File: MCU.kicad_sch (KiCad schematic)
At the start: 15 parts, among them U5 STM32F405RGTx, Y1 12MHz

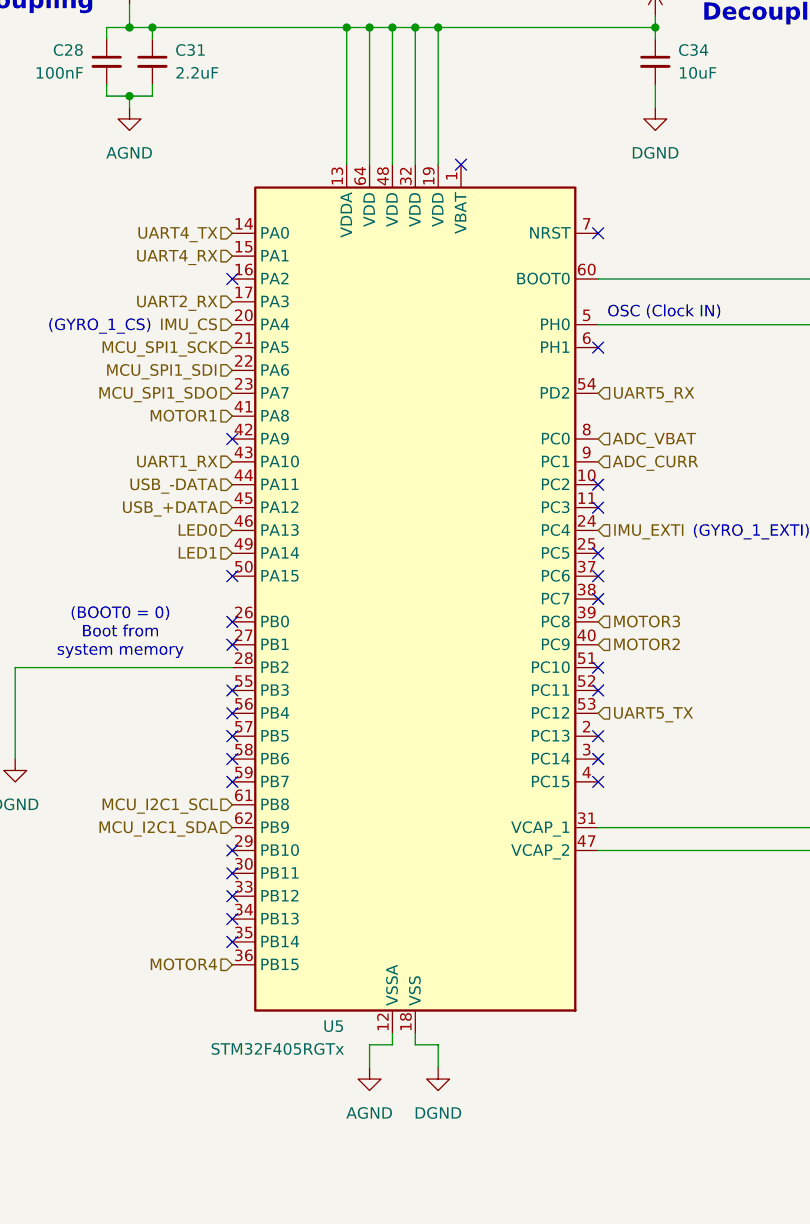
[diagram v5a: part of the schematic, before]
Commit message: More symbols updated to be compliant
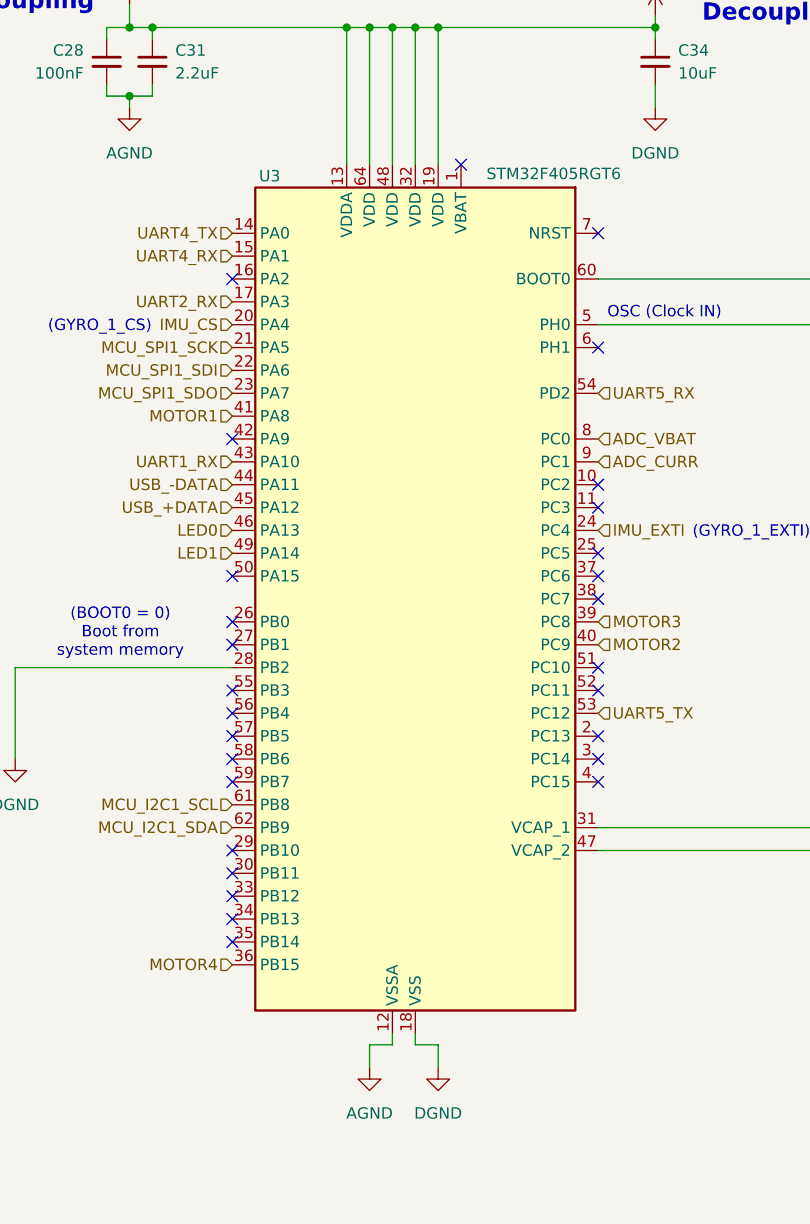
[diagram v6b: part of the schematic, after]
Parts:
- removed U5: STM32F405RGTx, Package_QFP:LQFP-64_10x10mm_P0.5mm, symbol MCU_ST_STM32F4:STM32F405RGTx
- added U3: STM32F405RGT6, Package_QFP:LQFP-64_10x10mm_P0.5mm, symbol KSE_MCU:STM32F405RGT6
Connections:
- net +3V3: now also U3.13 (VDDA), U3.19 (VDD), U3.32 (VDD), U3.48 (VDD), U3.64 (VDD)
- net ADC_CURR: now also U3.9 (PC1)
- net ADC_VBAT: now also U3.8 (PC0)
- net AGND: now also U3.12 (VSSA)
- net CLK_OUT: now also U3.5 (PH0)
- net DFU_Enable: now also U3.60 (BOOT0)
- net DGND: now also U3.18 (VSS), U3.28 (PB2), U3.63 (VSS)
- net IMU_CS: now also U3.20 (PA4)
- net IMU_EXTI: now also U3.24 (PC4)
- net LED0: now also U3.46 (PA13)
- net LED1: now also U3.49 (PA14)
- net MCU_I2C1_SCL: now also U3.61 (PB8)
- net MCU_I2C1_SDA: now also U3.62 (PB9)
- net MCU_SPI1_SCK: now also U3.21 (PA5)
- net MCU_SPI1_SDI: now also U3.22 (PA6)
- net MCU_SPI1_SDO: now also U3.23 (PA7)
- net MOTOR1: now also U3.41 (PA8)
- net MOTOR2: now also U3.40 (PC9)
- net MOTOR3: now also U3.39 (PC8)
- net MOTOR4: now also U3.36 (PB15)
- net UART1_RX: now also U3.43 (PA10)
- net UART2_RX: now also U3.17 (PA3)
- net UART4_RX: now also U3.15 (PA1)
- net UART4_TX: now also U3.14 (PA0)
- net UART5_RX: now also U3.54 (PD2)
- net UART5_TX: now also U3.53 (PC12)
- net USB_+DATA: now also U3.45 (PA12)
- net USB_-DATA: now also U3.44 (PA11)
- net at C30.1: now also U3.31 (VCAP_1)
- net at C29.1: now also U3.47 (VCAP_2)
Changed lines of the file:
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@@
+	)
+	(symbol
+		(lib_id "KSE_MCU:STM32F405RGT6")
+		(at 151.13 92.71 0)
+		(mirror y)
+		(unit 1)
+		(exclude_from_sim no)
+		(in_bom yes)
+		(on_board yes)
+		(dnp no)
+		(property "Reference" "U3"
+			(at 136.144 45.72 0)
+			(effects
+				(font
+					(size 1.27 1.27)
+				)
+				(justify left)
+			)
+		)
+		(property "Value" "STM32F405RGT6"
+			(at 173.99 45.466 0)
+			(effects
+				(font
+					(size 1.27 1.27)
+				)
+				(justify left)
+			)
+		)
+		(property "Footprint" "Package_QFP:LQFP-64_10x10mm_P0.5mm"
+			(at 168.91 138.43 0)
+			(effects
+				(font
+					(size 1.27 1.27)
+				)
+				(justify right)
+				(hide yes)
+			)
+		)
+		(property "Datasheet" "https://www.st.com/resource/en/datasheet/stm32f405rg.pdf"
+			(at 148.59 157.48 0)
+			(effects
+				(font
+					(size 1.27 1.27)
+				)
+				(hide yes)
+			)
+		)
+		(property "Description" "STMicroelectronics Arm Cortex-M4 MCU, 1024KB flash, 192KB RAM, 168 MHz, 1.8-3.6V, 51 GPIO, LQFP64"
+			(at 149.86 157.48 0)
+			(effects
+				(font
+					(size 1.27 1.27)
+				)
+				(hide yes)
+			)
+		)
+		(property "Manufacturer" "STMicroelectronics "
+			(at 149.352 156.464 0)
+			(effects
+				(font
+					(size 1.27 1.27)
+				)
+				(hide yes)
+			)
+		)
+		(property "MPN" "STM32F405RGT6 "
+			(at 151.892 157.48 0)
+			(effects
+				(font
+					(size 1.27 1.27)
+				)
+				(hide yes)
+			)
+		)
+		(pin "36"
+		)
+		(pin "33"
+		)
+		(pin "61"
+		)
+		(pin "35"
+		)
+		(pin "62"
+		)
+		(pin "30"
+		)
+		(pin "59"
+		)
+		(pin "29"
+		)
+		(pin "34"
+		)
+		(pin "6"
+		)
+		(pin "25"
+		)
+		(pin "9"
+		)
+		(pin "40"
+		)
+		(pin "52"
+		)
+		(pin "8"
+		)
+		(pin "53"
+		)
+		(pin "24"
+		)
+		(pin "32"
+		)
+		(pin "11"
+		)
+		(pin "31"
+		)
+		(pin "2"
+		)
+		(pin "54"
+		)
+		(pin "60"
+		)
+		(pin "5"
+		)
+		(pin "7"
+		)
+		(pin "10"
+		)
+		(pin "37"
+		)
+		(pin "38"
+		)
+		(pin "39"
+		)
+		(pin "51"
+		)
+		(pin "3"
+		)
+		(pin "4"
+		)
+		(pin "47"
+		)
+		(pin "1"
+		)
+		(pin "17"
+		)
+		(pin "19"
+		)
+		(pin "21"
+		)
+		(pin "56"
+		)
+		(pin "43"
+		)
+		(pin "18"
+		)
+		(pin "26"
+		)
+		(pin "13"
+		)
+		(pin "48"
+		)
+		(pin "42"
+		)
+		(pin "50"
+		)
+		(pin "14"
+		)
+		(pin "15"
+		)
+		(pin "12"
+		)
+		(pin "63"
+		)
+		(pin "22"
+		)
+		(pin "44"
+		)
+		(pin "23"
+		)
+		(pin "45"
+		)
+		(pin "27"
+		)
+		(pin "16"
+		)
+		(pin "20"
+		)
+		(pin "64"
+		)
+		(pin "41"
+		)
+		(pin "46"
+		)
+		(pin "28"
+		)
+		(pin "55"
+		)
+		(pin "49"
+		)
+		(pin "57"
+		)
+		(pin "58"
+		)
+		(instances
+			(project ""
+				(path "/f9e05184-c88b-4a88-ae9c-ab2bdb32be7c/c5103ceb-5325-4a84-a025-9638a412984e/6b8b8a56-80fd-4343-a336-2683563c3c7d"
+					(reference "U3")
+					(unit 1)
+				)
+			)
+		)
 	)
 	(symbol
@@
 					(unit 1)
 				)
-			)
-		)
-	)
-	(symbol
-		(lib_id "MCU_ST_STM32F4:STM32F405RGTx")
-		(at 151.13 92.71 0)
-		(mirror y)
-		(unit 1)
-		(exclude_from_sim no)
-		(in_bom yes)
-		(on_board yes)
-		(dnp no)
-		(property "Reference" "U5"
-			(at 143.256 140.208 0)
-			(effects
-				(font
-					(size 1.27 1.27)
-				)
-				(justify left)
-			)
-		)
-		(property "Value" "STM32F405RGTx"
-			(at 143.256 142.748 0)
-			(effects
-				(font
-					(size 1.27 1.27)
-				)
-				(justify left)
-			)
-		)
-		(property "Footprint" "Package_QFP:LQFP-64_10x10mm_P0.5mm"
-			(at 168.91 138.43 0)
-			(effects
-				(font
-					(size 1.27 1.27)
-				)
-				(justify right)
-				(hide yes)
-			)
-		)
-		(property "Datasheet" "https://www.st.com/resource/en/datasheet/stm32f405rg.pdf"
-			(at 151.13 92.71 0)
-			(effects
-				(font
-					(size 1.27 1.27)
-				)
-				(hide yes)
-			)
-		)
-		(property "Description" "STMicroelectronics Arm Cortex-M4 MCU, 1024KB flash, 192KB RAM, 168 MHz, 1.8-3.6V, 51 GPIO, LQFP64"
-			(at 151.13 92.71 0)
-			(effects
-				(font
-					(size 1.27 1.27)
-				)
-				(hide yes)
-			)
-		)
-		(pin "39"
-		)
-		(pin "37"
-		)
-		(pin "3"
-		)
-		(pin "1"
-		)
-		(pin "18"
-		)
-		(pin "2"
-		)
-		(pin "32"
-		)
-		(pin "4"
-		)
-		(pin "10"
-		)
-		(pin "31"
-		)
-		(pin "15"
-		)
-		(pin "8"
-		)
-		(pin "51"
-		)
-		(pin "7"
-		)
-		(pin "9"
-		)
-		(pin "11"
-		)
-		(pin "25"
-		)
-		(pin "60"
-		)
-		(pin "38"
-		)
-		(pin "52"
-		)
-		(pin "54"
-		)
-		(pin "5"
-		)
-		(pin "6"
-		)
-		(pin "24"
-		)
-		(pin "40"
-		)
-		(pin "53"
-		)
-		(pin "47"
-		)
-		(pin "19"
-		)
-		(pin "48"
-		)
-		(pin "63"
-		)
-		(pin "12"
-		)
-		(pin "64"
-		)
-		(pin "13"
-		)
-		(pin "14"
-		)
-		(pin "16"
-		)
-		(pin "30"
-		)
-		(pin "26"
-		)
-		(pin "55"
-		)
-		(pin "29"
-		)
-		(pin "57"
-		)
-		(pin "42"
-		)
-		(pin "20"
-		)
-		(pin "43"
-		)
-		(pin "21"
-		)
-		(pin "41"
-		)
-		(pin "44"
-		)
-		(pin "17"
-		)
-		(pin "22"
-		)
-		(pin "50"
-		)
-		(pin "23"
-		)
-		(pin "27"
-		)
-		(pin "28"
-		)
-		(pin "58"
-		)
-		(pin "59"
-		)
-		(pin "45"
-		)
-		(pin "49"
-		)
-		(pin "46"
-		)
-		(pin "61"
-		)
-		(pin "62"
-		)
-		(pin "56"
-		)
-		(pin "36"
-		)
-		(pin "34"
-		)
-		(pin "33"
-		)
-		(pin "35"
-		)
-		(instances
-			(project "FCU3"
-				(path "/f9e05184-c88b-4a88-ae9c-ab2bdb32be7c/c5103ceb-5325-4a84-a025-9638a412984e/6b8b8a56-80fd-4343-a336-2683563c3c7d"
-					(reference "U5")
-					(unit 1)
-				)

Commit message: Layout Draft Complete
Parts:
- S1: value TS32-7-35-BK-B-260-RA-SMT-TR -> NO; MPN (none) -> TS32-7-35-BK-B-260-RA-SMT-TR; Manufacturer (none) -> Same Sky
- Y1: footprint Crystal:Crystal_SMD_Abracon_ABM8AIG-4Pin_3.2x2.5mm -> KSE_passive:Crystal_SMD_Abracon_ABM8AIG-4Pin_3.2x2.5mm
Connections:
- net +3V3: now also S1.1; no longer S1.2
- net DFU_Enable: now also S1.2; no longer S1.1
- net DGND: now also S1.SH1 (MP), S1.SH2 (MP)
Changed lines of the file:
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@@
 	)
 	(junction
+		(at 257.81 55.88)
+		(diameter 0)
+		(color 0 0 0 0)
+	)
+	(junction
 		(at 257.81 48.26)
 		(diameter 0)
@@
 	(wire
 		(pts
+			(xy 257.81 55.88) (xy 257.81 57.15)
+		)
+		(stroke
+			(width 0)
+			(type default)
+		)
+	)
+	(wire
+		(pts
 			(xy 257.81 90.17) (xy 257.81 95.25)
 		)
@@
 	(wire
 		(pts
+			(xy 261.62 46.99) (xy 261.62 55.88)
+		)
+		(stroke
+			(width 0)
+			(type default)
+		)
+	)
+	(wire
+		(pts
 			(xy 143.51 29.21) (xy 143.51 44.45)
 		)
@@
 	(wire
 		(pts
-			(xy 257.81 54.61) (xy 257.81 58.42)
+			(xy 257.81 54.61) (xy 257.81 55.88)
 		)
 		(stroke
@@
 		)
 	)
+	(wire
+		(pts
+			(xy 261.62 55.88) (xy 257.81 55.88)
+		)
+		(stroke
+			(width 0)
+			(type default)
+		)
+	)
 	(label "DFU_Enable"
 		(at 232.41 48.26 0)
@@
 	(symbol
 		(lib_id "KSE_sensors:TS32-7-35-BK-B-260-RA-SMT-TR")
-		(at 257.81 39.37 90)
+		(at 257.81 39.37 0)
 		(unit 1)
 		(exclude_from_sim no)
@@
 		(on_board yes)
 		(dnp no)
-		(fields_autoplaced yes)
 		(property "Reference" "S1"
-			(at 259.08 38.0999 90)
+			(at 251.968 34.036 0)
 			(effects
 				(font
 					(size 1.27 1.27)
 				)
-				(justify right)
+				(justify left)
 			)
 		)
-		(property "Value" "TS32-7-35-BK-B-260-RA-SMT-TR"
-			(at 259.08 40.6399 90)
+		(property "Value" "NO"
+			(at 253.492 33.782 0)
 			(effects
 				(font
@@
 			)
 		)
-		(property "Datasheet" ""
+		(property "Datasheet" "https://eu.mouser.com/datasheet/3/6118/1/ts32.pdf"
 			(at 257.81 39.37 0)
 			(effects
@@
 			)
 		)
-		(property "Description" ""
+		(property "Description" "Tactile Switch SPST-NO Side Actuated Surface Mount, Right Angle"
 			(at 257.81 39.37 0)
 			(effects
@@
 			)
 		)
+		(property "Manufacturer" "Same Sky"
+			(at 259.08 71.628 0)
+			(effects
+				(font
+					(size 1.27 1.27)
+				)
+				(justify bottom)
+				(hide yes)
+			)
+		)
+		(property "MPN" "TS32-7-35-BK-B-260-RA-SMT-TR"
+			(at 258.826 65.532 0)
+			(effects
+				(font
+					(size 1.27 1.27)
+				)
+				(justify bottom)
+				(hide yes)
+			)
+		)
 		(pin "2"
 		)
 		(pin "1"
 		)
+		(pin "SH1"
+		)
+		(pin "SH2"
+		)
 		(instances
 			(project "FCU3"
@@
 	(symbol
 		(lib_id "power:+3.3V")
-		(at 257.81 31.75 0)
+		(at 257.81 33.02 0)
 		(mirror y)
 		(unit 1)
@@
 		(fields_autoplaced yes)
 		(property "Reference" "#PWR014"
-			(at 257.81 35.56 0)
+			(at 257.81 36.83 0)
 			(effects
 				(font
@@
 		)
 		(property "Value" "+3V3"
-			(at 257.81 26.67 0)
+			(at 257.81 27.94 0)
 			(effects
 				(font
@@
 		)
 		(property "Footprint" ""
-			(at 257.81 31.75 0)
+			(at 257.81 33.02 0)
 			(effects
 				(font
@@
 		)
 		(property "Datasheet" ""
-			(at 257.81 31.75 0)
+			(at 257.81 33.02 0)
 			(effects
 				(font
@@
 		)
 		(property "Description" "Power symbol creates a global label with name \"+3.3V\""
-			(at 257.81 31.75 0)
+			(at 257.81 33.02 0)
 			(effects
 				(font
@@
 			)
 		)
-		(property "Footprint" "Crystal:Crystal_SMD_Abracon_ABM8AIG-4Pin_3.2x2.5mm"
+		(property "Footprint" "KSE_passive:Crystal_SMD_Abracon_ABM8AIG-4Pin_3.2x2.5mm"
 			(at 257.81 85.09 0)
 			(effects
@@
 		(lib_id "KSE_Resistors:R_Small")
 		(at 257.81 52.07 0)
+		(mirror y)
 		(unit 1)
 		(exclude_from_sim no)
@@
 		(on_board yes)
 		(dnp no)
-		(fields_autoplaced yes)
 		(property "Reference" "R8"
-			(at 260.35 50.7999 0)
+			(at 255.27 50.7999 0)
 			(effects
 				(font
@@
 		)
 		(property "Value" "10k"
-			(at 260.35 53.3399 0)
+			(at 255.27 53.3399 0)
 			(effects
 				(font
@@
 	(symbol
 		(lib_id "power:GND2")
-		(at 257.81 58.42 0)
+		(at 257.81 57.15 0)
 		(mirror y)
 		(unit 1)
@@
 		(fields_autoplaced yes)
 		(property "Reference" "#PWR016"
-			(at 257.81 64.77 0)
+			(at 257.81 63.5 0)
 			(effects
 				(font
@@
 		)
 		(property "Value" "DGND"
-			(at 257.81 63.5 0)
+			(at 257.81 62.23 0)
 			(effects
 				(font
@@
 		)
 		(property "Footprint" ""
-			(at 257.81 58.42 0)
+			(at 257.81 57.15 0)
 			(effects
 				(font
@@
 		)
 		(property "Datasheet" ""
-			(at 257.81 58.42 0)
+			(at 257.81 57.15 0)
 			(effects
 				(font
@@
 		)
 		(property "Description" "Power symbol creates a global label with name \"GND2\" , ground"
-			(at 257.81 58.42 0)
+			(at 257.81 57.15 0)
 			(effects
 				(font

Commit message: DRC/ERC Remaining
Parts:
- added J2: ST-LINK_Header, Connector_PinHeader_1.27mm:PinHeader_2x03_P1.27mm_Vertical_SMD, symbol KSE_connectors:ST-LINK_Header
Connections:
- net +3V3: now also J2.1 (Pin_1)
- net DGND: now also J2.3 (Pin_3), J2.5 (Pin_5)
- net SWO: now reaches U3.55 (PB3)
- net SWO: now also J2.6 (Pin_6)
- net LED0 renamed SWDIO
- net SWDIO: now also J2.2 (Pin_2)
- net LED1 renamed SWCLK
- net SWCLK: now also J2.4 (Pin_4)
- no-connect marks 28 -> 27
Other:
- note added: "GND"
- note added: "ST-Link Debugger"
- note added: "SWCLK"
- note added: "SWDIO"
- note added: "SWO"
- note added: "VCC"
